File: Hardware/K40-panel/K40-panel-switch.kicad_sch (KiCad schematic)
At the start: 2 parts

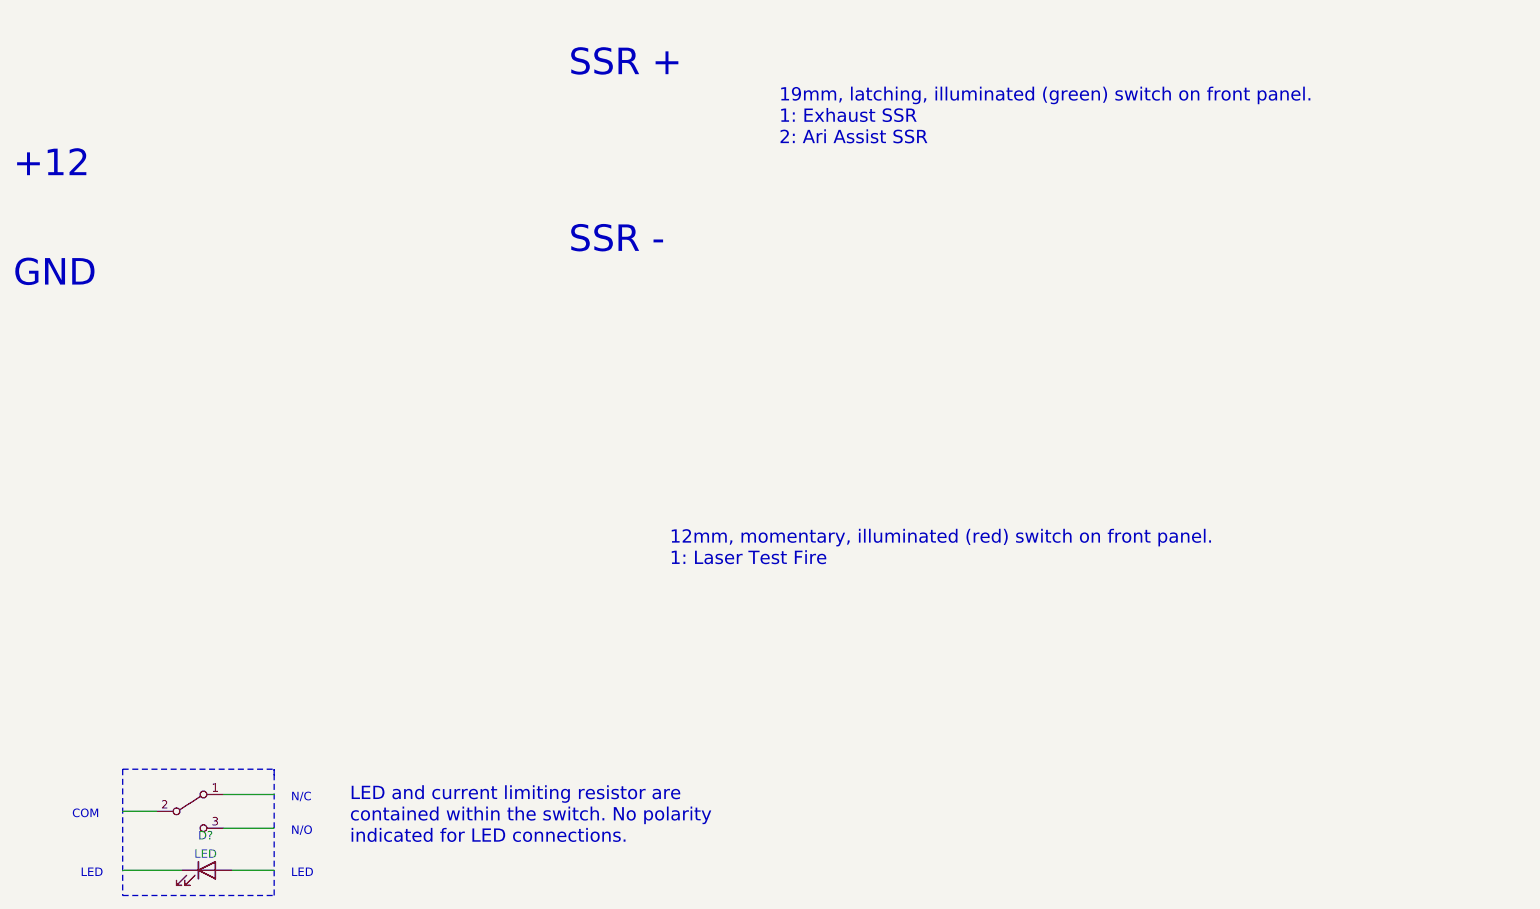
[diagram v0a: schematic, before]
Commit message: Changes to be committed: 	new file:   K40-panel/K40-panel-switch.kicad_sch 	modified:   K40-panel/K40-panel.kicad_sch 	modified:   K40-panel/switch.kicad_sch Renamed to K40-panel-switch.kicad_sch 	modified:   K40-power/K40-power.kicad_prl 	modified:   K40-power/K40-power.kicad_sch Updated symbols, added notes about auxillary power supply
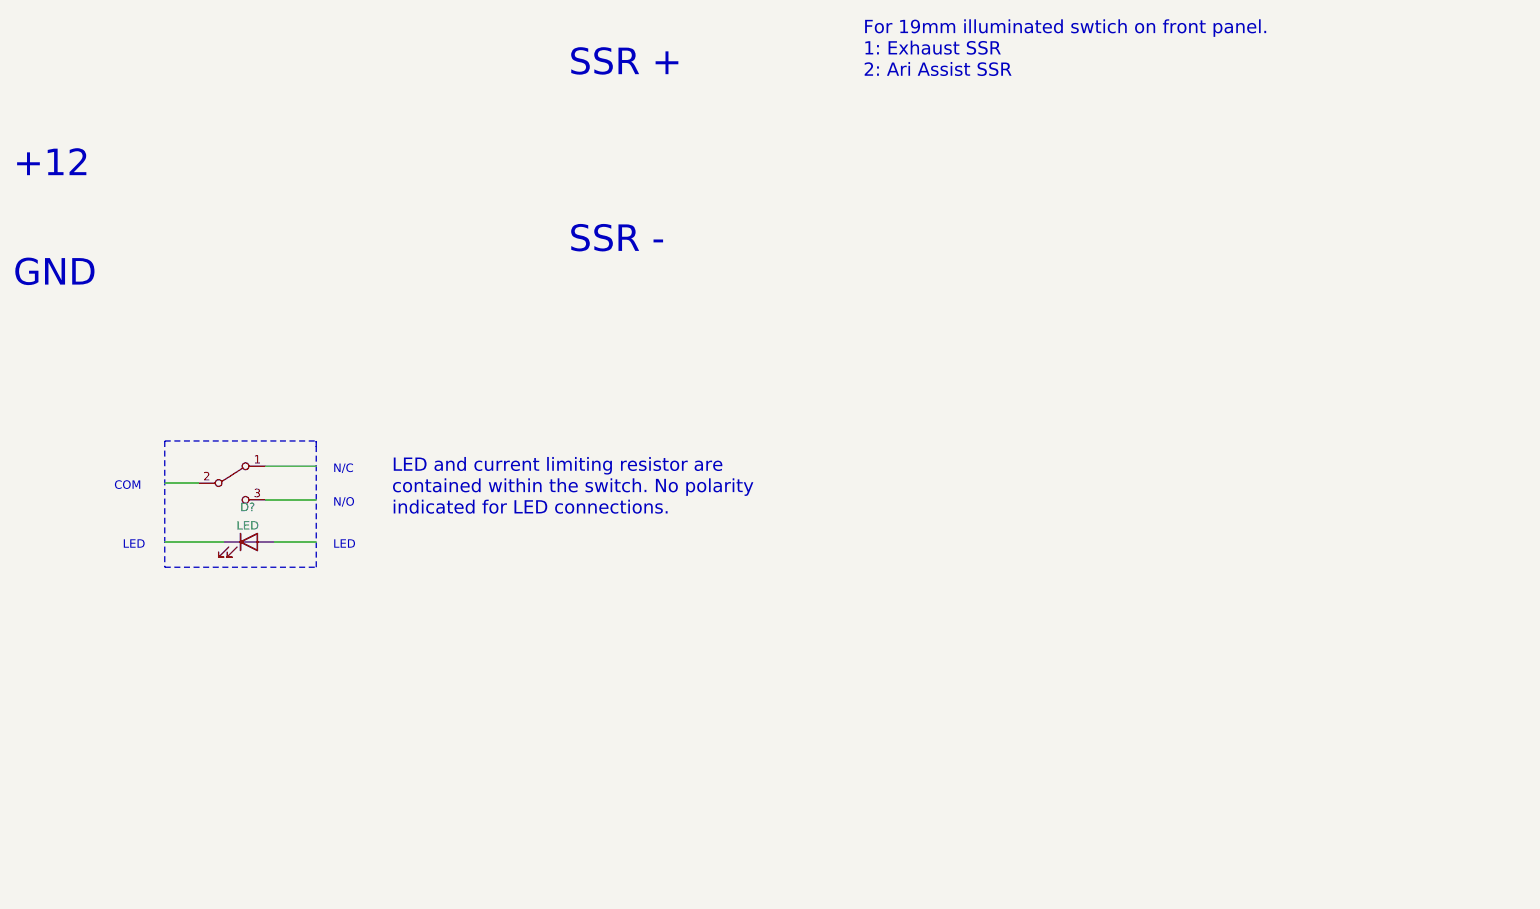
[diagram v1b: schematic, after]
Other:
- note added: "For 19mm illuminated swtich on front panel. 1: Exhaust SSR 2: Ari Assist SSR"
- note removed: "12mm, momentary, illuminated (red) switch on front panel. 1: Laser Test Fire"
- note removed: "19mm, latching, illuminated (green) switch on front panel. 1: Exhaust SSR 2: Ari Assist SSR"
- moved on the sheet: D?
